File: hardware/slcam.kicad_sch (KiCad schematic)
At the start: 36 parts, among them J1 53261-0671, J2 Conn_01x08, J3 Conn_01x04, J4 53261-0371, J5 53261-0371, U1 STM32F103C8Tx, U2 W25Q128JVS, U3 TCAN330G, U4 TPS2044D, Y1 Crystal_GND24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

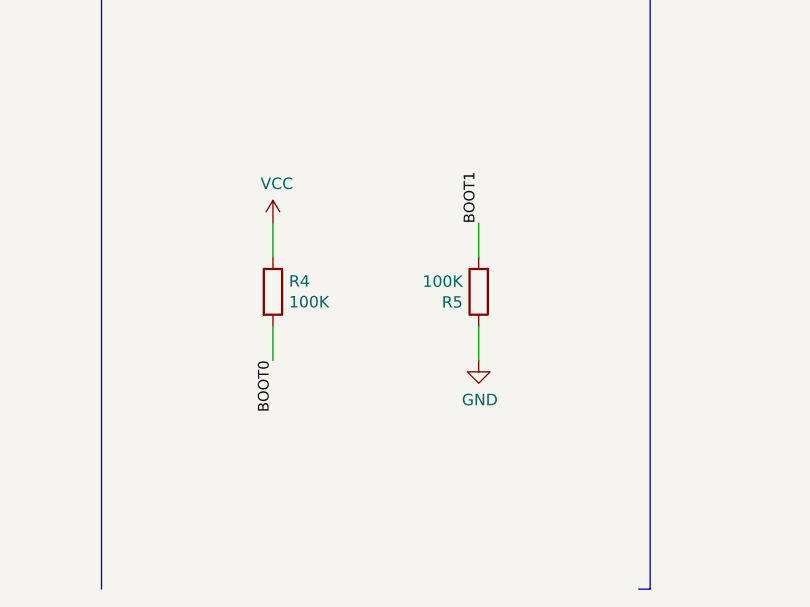
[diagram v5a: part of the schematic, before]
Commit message: hardware: Fixing the boot mode option (changing to main flash memory)
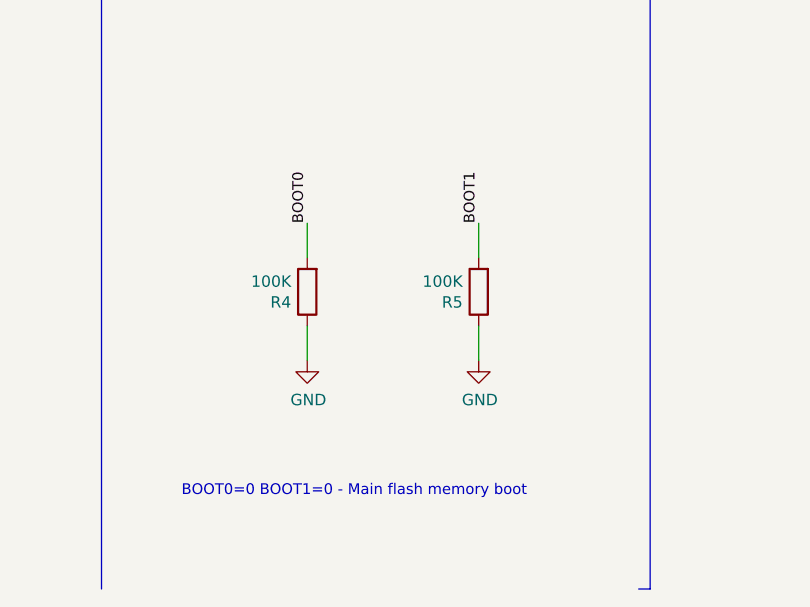
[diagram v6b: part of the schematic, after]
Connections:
- net GND: now also R4.1
- net VCC: no longer R4.1
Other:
- note added: "BOOT0=0 BOOT1=0 - Main flash memory boot"
- moved on the sheet: R4
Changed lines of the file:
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@@
   (title_block
     (title "SLCam")
-    (date "2023-05-09")
+    (date "2023-05-11")
     (rev "v0.2")
     (company "Space Technology Research Laboratory - SpaceLab")
@@
     (stroke (width 0) (type default) (color 0 0 0 0))
   )
+  (wire (pts (xy 111.76 256.54) (xy 111.76 260.35))
+    (stroke (width 0) (type default) (color 0 0 0 0))
+  )
   (wire (pts (xy 285.75 256.54) (xy 285.75 257.81))
     (stroke (width 0) (type default) (color 0 0 0 0))
@@
     (stroke (width 0) (type default) (color 0 0 0 0))
   )
-  (wire (pts (xy 107.95 245.11) (xy 107.95 248.92))
-    (stroke (width 0) (type default) (color 0 0 0 0))
-  )
   (polyline (pts (xy 299.72 210.82) (xy 407.67 210.82))
     (stroke (width 0) (type default) (color 0 0 0 0))
@@
     (stroke (width 0) (type default) (color 0 0 0 0))
   )
+  (wire (pts (xy 111.76 245.11) (xy 111.76 248.92))
+    (stroke (width 0) (type default) (color 0 0 0 0))
+  )
   (wire (pts (xy 105.41 135.89) (xy 119.38 135.89))
-    (stroke (width 0) (type default) (color 0 0 0 0))
-  )
-  (wire (pts (xy 107.95 256.54) (xy 107.95 260.35))
     (stroke (width 0) (type default) (color 0 0 0 0))
   )
@@
     (effects (font (size 5.0038 5.0038)) (justify left bottom))
   )
+  (text "BOOT0=0 BOOT1=0 - Main flash memory boot" (at 97.79 275.59 0)
+    (effects (font (size 1.1938 1.1938)) (justify left bottom))
+  )
   (text "Connectors" (at 309.88 25.4 0)
     (effects (font (size 5.0038 5.0038)) (justify left bottom))
@@
     (effects (font (size 1.1938 1.1938)) (justify right bottom))
   )
-  (label "BOOT0" (at 107.95 260.35 270)
-    (effects (font (size 1.1938 1.1938)) (justify right bottom))
+  (label "BOOT0" (at 111.76 245.11 90)
+    (effects (font (size 1.1938 1.1938)) (justify left bottom))
   )
   (label "I2C_SDA" (at 193.04 260.35 270)
@@
     (pin "1")
   )
-  (symbol (lib_id "Device:R") (at 107.95 252.73 0) (unit 1)
-    (in_bom yes) (on_board yes)
-    (property "Reference" "R4" (id 0) (at 109.728 251.5616 0)
-      (effects (font (size 1.27 1.27)) (justify left))
-    )
-    (property "Value" "100K" (id 1) (at 109.728 253.873 0)
-      (effects (font (size 1.27 1.27)) (justify left))
-    )
-    (property "Footprint" "Resistor_SMD:R_0603_1608Metric_Pad1.05x0.95mm_HandSolder" (id 2) (at 106.172 252.73 90)
-      (effects (font (size 1.27 1.27)) hide)
-    )
-    (property "Datasheet" "~" (id 3) (at 107.95 252.73 0)
-      (effects (font (size 1.27 1.27)) hide)
-    )
-    (property "Partnumber" "MCT0603MC1003FP500" (id 4) (at 107.95 252.73 0)
+  (symbol (lib_id "Device:R") (at 111.76 252.73 180) (unit 1)
+    (in_bom yes) (on_board yes)
+    (property "Reference" "R4" (id 0) (at 109.982 253.8984 0)
+      (effects (font (size 1.27 1.27)) (justify left))
+    )
+    (property "Value" "100K" (id 1) (at 109.982 251.587 0)
+      (effects (font (size 1.27 1.27)) (justify left))
+    )
+    (property "Footprint" "Resistor_SMD:R_0603_1608Metric_Pad1.05x0.95mm_HandSolder" (id 2) (at 113.538 252.73 90)
+      (effects (font (size 1.27 1.27)) hide)
+    )
+    (property "Datasheet" "~" (id 3) (at 111.76 252.73 0)
+      (effects (font (size 1.27 1.27)) hide)
+    )
+    (property "Partnumber" "MCT0603MC1003FP500" (id 4) (at 111.76 252.73 0)
       (effects (font (size 1.27 1.27)) hide)
     )
@@
     )
     (property "Datasheet" "" (id 3) (at 130.81 260.35 0)
-      (effects (font (size 1.27 1.27)) hide)
-    )
-    (pin "1")
-  )
-  (symbol (lib_id "power:VCC") (at 107.95 245.11 0) (unit 1)
-    (in_bom yes) (on_board yes)
-    (property "Reference" "#PWR01" (id 0) (at 107.95 248.92 0)
-      (effects (font (size 1.27 1.27)) hide)
-    )
-    (property "Value" "VCC" (id 1) (at 108.3818 240.7158 0))
-    (property "Footprint" "" (id 2) (at 107.95 245.11 0)
-      (effects (font (size 1.27 1.27)) hide)
-    )
-    (property "Datasheet" "" (id 3) (at 107.95 245.11 0)
       (effects (font (size 1.27 1.27)) hide)
     )
@@
     (pin "1")
     (pin "2")
+  )
+  (symbol (lib_id "power:GND") (at 111.76 260.35 0) (unit 1)
+    (in_bom yes) (on_board yes)
+    (property "Reference" "#PWR?" (id 0) (at 111.76 266.7 0)
+      (effects (font (size 1.27 1.27)) hide)
+    )
+    (property "Value" "GND" (id 1) (at 111.887 264.7442 0))
+    (property "Footprint" "" (id 2) (at 111.76 260.35 0)
+      (effects (font (size 1.27 1.27)) hide)
+    )
+    (property "Datasheet" "" (id 3) (at 111.76 260.35 0)
+      (effects (font (size 1.27 1.27)) hide)
+    )
+    (pin "1")
   )
   (symbol (lib_id "power:VCC") (at 208.28 59.69 90) (unit 1)
@@
       (reference "#FLG0102") (unit 1) (value "PWR_FLAG") (footprint "")
     )
-    (path "/00000000-0000-0000-0000-0000632037f5"
-      (reference "#PWR01") (unit 1) (value "VCC") (footprint "")
-    )
     (path "/00000000-0000-0000-0000-0000631ff042"
       (reference "#PWR02") (unit 1) (value "GND") (footprint "")
@@
       (reference "#PWR0109") (unit 1) (value "GND") (footprint "")
     )
+    (path "/6e76eb2d-fc74-4d5a-9200-eb229c175f06"
+      (reference "#PWR?") (unit 1) (value "GND") (footprint "")
+    )
     (path "/00000000-0000-0000-0000-00006313d384"

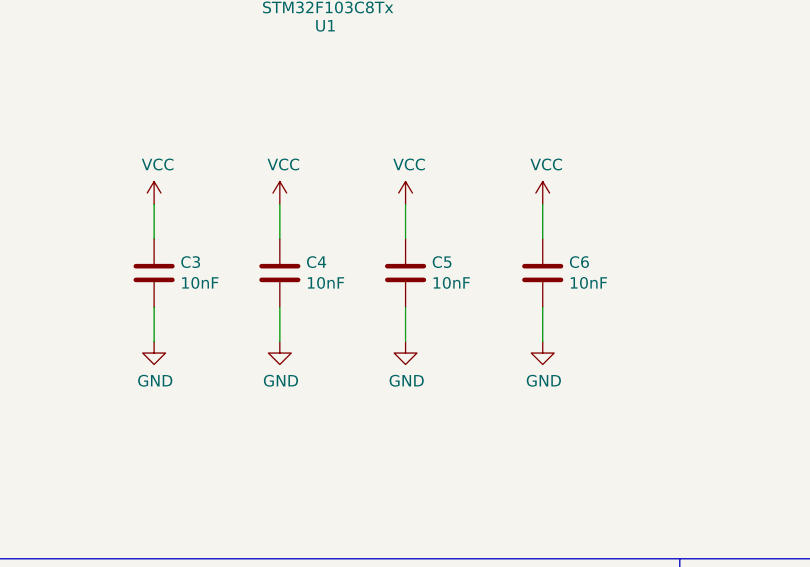
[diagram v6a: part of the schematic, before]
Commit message: hardware: Fixing the value of some capacitors
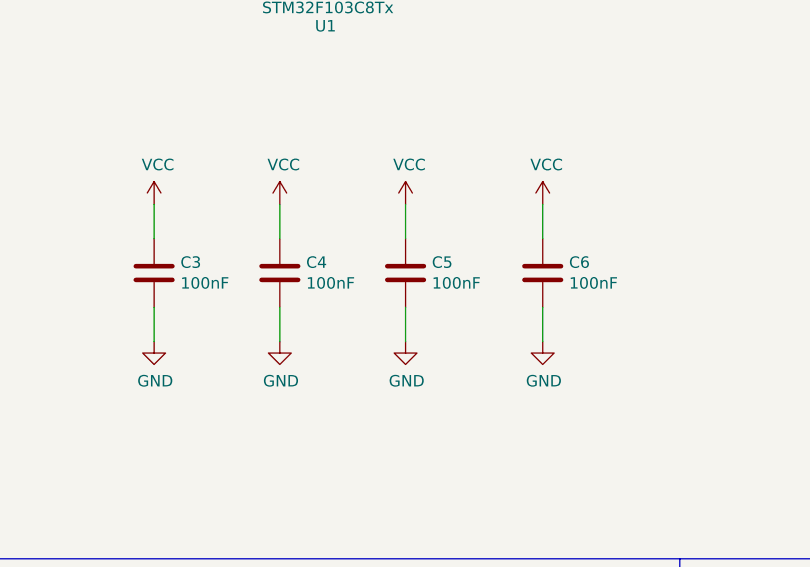
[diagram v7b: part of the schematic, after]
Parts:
- C3, C4, C5, C6: value 10nF -> 100nF; Partnumber VJ0603Y103KXJAC31X -> C0603C104K5RAC3121
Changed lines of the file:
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@@
       (effects (font (size 1.27 1.27)) (justify left))
     )
-    (property "Value" "10nF" (id 1) (at 47.371 180.213 0)
+    (property "Value" "100nF" (id 1) (at 47.371 180.213 0)
       (effects (font (size 1.27 1.27)) (justify left))
     )
@@
       (effects (font (size 1.27 1.27)) hide)
     )
-    (property "Partnumber" "VJ0603Y103KXJAC31X" (id 4) (at 44.45 179.07 0)
+    (property "Partnumber" "C0603C104K5RAC3121" (id 4) (at 44.45 179.07 0)
       (effects (font (size 1.27 1.27)) hide)
     )
@@
       (effects (font (size 1.27 1.27)) (justify left))
     )
-    (property "Value" "10nF" (id 1) (at 61.341 180.213 0)
+    (property "Value" "100nF" (id 1) (at 61.341 180.213 0)
       (effects (font (size 1.27 1.27)) (justify left))
     )
@@
       (effects (font (size 1.27 1.27)) hide)
     )
-    (property "Partnumber" "VJ0603Y103KXJAC31X" (id 4) (at 58.42 179.07 0)
+    (property "Partnumber" "C0603C104K5RAC3121" (id 4) (at 58.42 179.07 0)
       (effects (font (size 1.27 1.27)) hide)
     )
@@
       (effects (font (size 1.27 1.27)) (justify left))
     )
-    (property "Value" "10nF" (id 1) (at 76.581 180.213 0)
+    (property "Value" "100nF" (id 1) (at 76.581 180.213 0)
       (effects (font (size 1.27 1.27)) (justify left))
     )
@@
       (effects (font (size 1.27 1.27)) hide)
     )
-    (property "Partnumber" "VJ0603Y103KXJAC31X" (id 4) (at 73.66 179.07 0)
+    (property "Partnumber" "C0603C104K5RAC3121" (id 4) (at 73.66 179.07 0)
       (effects (font (size 1.27 1.27)) hide)
     )
@@
       (effects (font (size 1.27 1.27)) (justify left))
     )
-    (property "Value" "10nF" (id 1) (at 33.401 180.213 0)
+    (property "Value" "100nF" (id 1) (at 33.401 180.213 0)
       (effects (font (size 1.27 1.27)) (justify left))
     )
@@
       (effects (font (size 1.27 1.27)) hide)
     )
-    (property "Partnumber" "VJ0603Y103KXJAC31X" (id 4) (at 30.48 179.07 0)
+    (property "Partnumber" "C0603C104K5RAC3121" (id 4) (at 30.48 179.07 0)
       (effects (font (size 1.27 1.27)) hide)
     )
@@
     )
     (path "/00000000-0000-0000-0000-00006369933b"
-      (reference "C3") (unit 1) (value "10nF") (footprint "Capacitor_SMD:C_0603_1608Metric_Pad1.05x0.95mm_HandSolder")
+      (reference "C3") (unit 1) (value "100nF") (footprint "Capacitor_SMD:C_0603_1608Metric_Pad1.05x0.95mm_HandSolder")
     )
     (path "/00000000-0000-0000-0000-00006366f149"
-      (reference "C4") (unit 1) (value "10nF") (footprint "Capacitor_SMD:C_0603_1608Metric_Pad1.05x0.95mm_HandSolder")
+      (reference "C4") (unit 1) (value "100nF") (footprint "Capacitor_SMD:C_0603_1608Metric_Pad1.05x0.95mm_HandSolder")
     )
     (path "/00000000-0000-0000-0000-000063692e92"
-      (reference "C5") (unit 1) (value "10nF") (footprint "Capacitor_SMD:C_0603_1608Metric_Pad1.05x0.95mm_HandSolder")
+      (reference "C5") (unit 1) (value "100nF") (footprint "Capacitor_SMD:C_0603_1608Metric_Pad1.05x0.95mm_HandSolder")
     )
     (path "/00000000-0000-0000-0000-0000636960f0"
-      (reference "C6") (unit 1) (value "10nF") (footprint "Capacitor_SMD:C_0603_1608Metric_Pad1.05x0.95mm_HandSolder")
+      (reference "C6") (unit 1) (value "100nF") (footprint "Capacitor_SMD:C_0603_1608Metric_Pad1.05x0.95mm_HandSolder")
     )
     (path "/00000000-0000-0000-0000-0000636ef5dc"
